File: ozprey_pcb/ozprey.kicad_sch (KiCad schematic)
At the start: 3 parts, among them J1 Conn_01x02, SW43 SW_DPDT_x2, U1 nice_nano

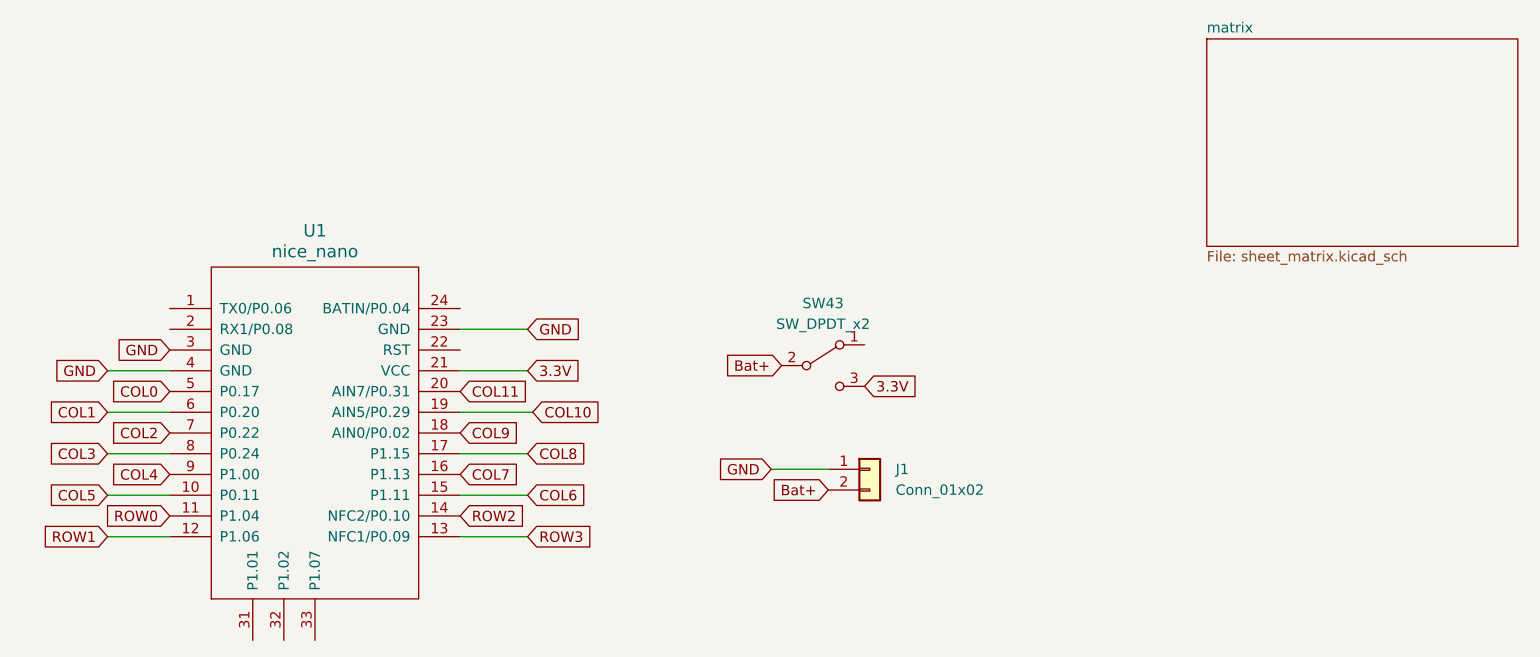
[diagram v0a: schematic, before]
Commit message: rework pcb, remove enclosure & plate folders
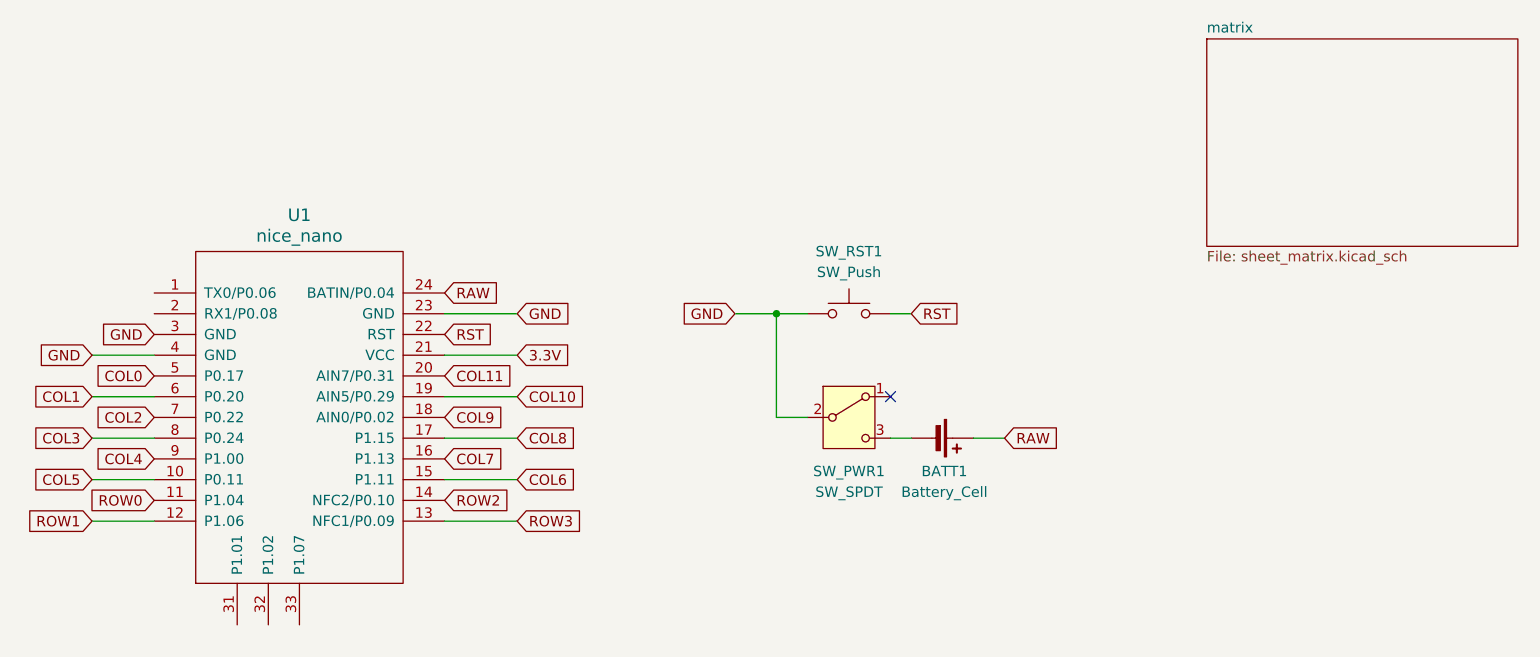
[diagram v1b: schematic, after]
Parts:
- removed J1: Conn_01x02, Connector_JST:JST_ACH_BM02B-ACHSS-GAN-ETF_1x02-1MP_P1.20mm_Vertical, symbol Connector_Generic:Conn_01x02
- removed SW43: SW_DPDT_x2, kapee-keeb-parts:MSK12C02, symbol Switch:SW_SPDT
- added BATT1: Battery_Cell, Keyboard:Battery_pads, symbol Device:Battery_Cell
- added SW_PWR1: SW_SPDT, Button_Switch_SMD:SW_SPDT_PCM12, symbol Switch:SW_SPDT
- added SW_RST1: SW_Push, Button_Switch_SMD:SW_SPST_TL3342, symbol Switch:SW_Push
- U1: footprint kapee-keeb-parts:NiceNano -> ProMicro:nice_nano
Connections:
- net GND: now also SW_PWR1.2 (B), SW_RST1.1
- net RST: now reaches U1.22 (RST)
- net RST: now also SW_RST1.2
- net RAW: now reaches U1.24 (BATIN/P0.04)
- net RAW: now also BATT1.1 (+)
- new net: BATT1.2 (-), SW_PWR1.3 (C)
- no-connect marks 0 -> 1
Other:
- company: (none) -> itsdmd
- title: (none) -> Ozprey
- moved on the sheet: U1

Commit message: update doc
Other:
- sheet matrix renamed Matrix
- added sheet MountingHoles (untitled.kicad_sch)
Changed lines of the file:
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@@
 			(color 0 0 0 0.0000)
 		)
-		(property "Sheetname" "matrix"
-			(at 187.325 24.1295 0)
+		(property "Sheetname" "Matrix"
+			(at 187.325 24.0534 0)
 			(effects
 				(font
@@
 		)
 		(property "Sheetfile" "sheet_matrix.kicad_sch"
-			(at 187.325 50.6735 0)
+			(at 187.325 50.7496 0)
 			(effects
 				(font
+					(size 1.27 1.27)
+				)
+				(justify left top)
+			)
+		)
+		(instances
+			(project "ozprey"
+				(path "/86a516b3-939b-48ee-9a25-d0111c577d06"
+					(page "2")
+				)
+			)
+		)
+	)
+	(sheet
+		(at 187.96 59.69)
+		(size 38.1 24.13)
+		(fields_autoplaced yes)
+		(stroke
+			(width 0.1524)
+			(type solid)
+		)
+		(fill
+			(color 0 0 0 0.0000)
+		)
+		(property "Sheetname" "MountingHoles"
+			(at 187.96 58.9784 0)
+			(effects
+				(font
+					(size 1.27 1.27)
+				)
+				(justify left bottom)
+			)
+		)
+		(property "Sheetfile" "untitled.kicad_sch"
+			(at 187.96 84.4046 0)
+			(effects
+				(font

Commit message: replace power & reset switches
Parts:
- removed SW_PWR1: SW_SPDT, Button_Switch_SMD:SW_SPDT_PCM12, symbol Switch:SW_SPDT
- added SW43: SK12D07VG4, Switch:SK12D07VG4, symbol SK12D07VG4:SK12D07VG4
- SW_RST1: footprint Button_Switch_SMD:SW_SPST_TL3342 -> Switch:KG1
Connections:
- net GND: now also SW_RST1.2, SW43.COM; no longer SW_RST1.1
- net RST: now also SW_RST1.1; no longer SW_RST1.2
- net at BATT1.2 (-): now also SW43.2
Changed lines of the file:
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@@
+		(color 0 0 0 0)
+	)
+	(junction
+		(at 135.89 71.12)
+		(diameter 0)
 		(color 0 0 0 0)
 	)
@@
 	(wire
 		(pts
+			(xy 135.89 71.12) (xy 138.43 71.12)
+		)
+		(stroke
+			(width 0)
+			(type default)
+		)
+	)
+	(wire
+		(pts
 			(xy 93.98 68.58) (xy 102.87 68.58)
 		)
@@
 	(wire
 		(pts
+			(xy 134.62 71.12) (xy 135.89 71.12)
+		)
+		(stroke
+			(width 0)
+			(type default)
+		)
+	)
+	(wire
+		(pts
 			(xy 93.98 78.74) (xy 102.87 78.74)
 		)
@@
 		(pts
 			(xy 50.8 73.66) (xy 58.42 73.66)
-		)
-		(stroke
-			(width 0)
-			(type default)
-		)
-	)
-	(wire
-		(pts
-			(xy 134.62 71.12) (xy 138.43 71.12)
 		)
 		(stroke
@@
 	)
 	(symbol
-		(lib_name "SW_SPDT_1")
-		(lib_id "Switch:SW_SPDT")
-		(at 143.51 71.12 0)
-		(unit 1)
-		(exclude_from_sim no)
-		(in_bom yes)
-		(on_board yes)
-		(dnp no)
-		(property "Reference" "SW_PWR1"
-			(at 143.51 77.724 0)
-			(effects
-				(font
-					(size 1.27 1.27)
-				)
-			)
-		)
-		(property "Value" "SW_SPDT"
-			(at 143.51 80.264 0)
-			(effects
-				(font
-					(size 1.27 1.27)
-				)
-			)
-		)
-		(property "Footprint" "Button_Switch_SMD:SW_SPDT_PCM12"
-			(at 143.51 71.12 0)
-			(effects
-				(font
-					(size 1.27 1.27)
-				)
-				(hide yes)
-			)
-		)
-		(property "Datasheet" "~"
-			(at 143.51 78.74 0)
-			(effects
-				(font
-					(size 1.27 1.27)
-				)
-				(hide yes)
-			)
-		)
-		(property "Description" "Switch, single pole double throw"
-			(at 143.51 71.12 0)
-			(effects
-				(font
-					(size 1.27 1.27)
-				)
-				(hide yes)
-			)
-		)
-		(pin "2"
-		)
-		(pin "1"
-		)
-		(pin "3"
-		)
-		(instances
-			(project ""
-				(path "/86a516b3-939b-48ee-9a25-d0111c577d06"
-					(reference "SW_PWR1")
-					(unit 1)
-				)
-			)
-		)
-	)
-	(symbol
 		(lib_id "nice_nano:nice_nano")
 		(at 76.2 69.85 0)
@@
 		(lib_id "Switch:SW_Push")
 		(at 143.51 58.42 0)
+		(mirror y)
 		(unit 1)
 		(exclude_from_sim no)
@@
 			)
 		)
-		(property "Footprint" "Button_Switch_SMD:SW_SPST_TL3342"
+		(property "Footprint" "Switch:KG1"
 			(at 143.51 53.34 0)
 			(effects
@@
 					(unit 1)
 				)
+			)
+		)
+	)
+	(symbol
+		(lib_id "SK12D07VG4:SK12D07VG4")
+		(at 142.24 72.39 0)
+		(unit 1)
+		(exclude_from_sim no)
+		(in_bom yes)
+		(on_board yes)
+		(dnp no)
+		(property "Reference" "SW43"
+			(at 142.24 77.724 0)
+			(effects
+				(font
+					(size 1.27 1.27)
+				)
+			)
+		)
+		(property "Value" "SK12D07VG4"
+			(at 142.24 80.264 0)
+			(effects
+				(font
+					(size 1.27 1.27)
+				)
+			)
+		)
+		(property "Footprint" "Switch:SK12D07VG4"
+			(at 142.24 80.772 0)
+			(effects
+				(font
+					(size 1.27 1.27)
+				)
+				(justify bottom)
+				(hide yes)
+			)
+		)
+		(property "Datasheet" ""
+			(at 142.24 72.39 0)
+			(effects
+				(font
+					(size 1.27 1.27)
+				)
+				(hide yes)
+			)
+		)
+		(property "Description" ""
+			(at 142.24 72.39 0)
+			(effects
+				(font
+					(size 1.27 1.27)
+				)
+				(hide yes)
+			)
+		)
+		(property "MF" "C&K"
+			(at 142.24 72.39 0)
+			(effects
+				(font
+					(size 1.27 1.27)
+				)
+				(justify bottom)
+				(hide yes)
+			)
+		)
+		(property "Description_1" "\nSwitch Slide ON ON SPDT Side Slide 0.3A 30VDC PC Pins Bracket Mount/Through Hole Bulk\n"
+			(at 142.748 86.614 0)
+			(effects
+				(font
+					(size 1.27 1.27)
+				)
+				(justify bottom)
+				(hide yes)
+			)
+		)
+		(property "Package" "None"
+			(at 142.24 72.39 0)
+			(effects
+				(font
+					(size 1.27 1.27)
+				)
+				(justify bottom)
+				(hide yes)
+			)
+		)
+		(property "Price" "None"
+			(at 142.24 72.39 0)
+			(effects
+				(font
+					(size 1.27 1.27)
+				)
+				(justify bottom)
+				(hide yes)
+			)
+		)
+		(property "SnapEDA_Link" "https://www.snapeda.com/parts/SK12D07VG4/C%2526K/view-part/?ref=snap"
+			(at 142.494 84.836 0)
+			(effects
+				(font
+					(size 1.27 1.27)
+				)
+				(justify bottom)
+				(hide yes)
+			)
+		)
+		(property "MP" "SK12D07VG4"
+			(at 141.986 78.486 0)
+			(effects
+				(font
+					(size 1.27 1.27)
+				)
+				(justify bottom)
+				(hide yes)
+			)
+		)
+		(property "Availability" "Not in stock"
+			(at 142.24 72.39 0)
+			(effects
+				(font
+					(size 1.27 1.27)
+				)
+				(justify bottom)
+				(hide yes)
+			)
+		)
+		(property "Check_prices" "https://www.snapeda.com/parts/SK12D07VG4/C%2526K/view-part/?ref=eda"
+			(at 141.986 82.804 0)
+			(effects
+				(font
+					(size 1.27 1.27)
+				)
+				(justify bottom)
+				(hide yes)
+			)
+		)
+		(pin "COM"
+		)
+		(pin "1"
+		)
+		(pin "2"
+		)
+		(instances
+			(project ""
+				(path "/86a516b3-939b-48ee-9a25-d0111c577d06"
+					(reference "SW43")
+					(unit 1)
+				)

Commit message: major changes, add plate
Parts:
- added SW_RST2: SW_Push, itsdmd:SW-T_SPST_TL3342, symbol Switch:SW_Push
- BATT1: footprint Keyboard:Battery_pads -> itsdmd:Battery_Pads-dual-side
- SW43: footprint Switch:SK12D07VG4 -> itsdmd:SW-S_SK12D07VG4; symbol SK12D07VG4:SK12D07VG4 -> itsdmd:SK12D07VG4
- SW_RST1: footprint Switch:KG1 -> itsdmd:SW-S_7.4x2.6-4pad-smd
- U1: footprint ProMicro:nice_nano -> itsdmd:MCB_nice-nano_flip; symbol nice_nano:nice_nano -> itsdmd:nice_nano; now left out of the parts list
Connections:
- net COL0: now also U1.20 (P0.31-LF); no longer U1.5 (P0.17)
- net COL1: now also U1.19 (P0.29-LF); no longer U1.6 (P0.20)
- net COL10: now also U1.6 (P0.20); no longer U1.19 (AIN5/P0.29)
- net COL11: now also U1.5 (P0.17); no longer U1.20 (AIN7/P0.31)
- net COL2: now also U1.18 (P0.02-LF); no longer U1.7 (P0.22)
- net COL3: now also U1.17 (P1.15-LF); no longer U1.8 (P0.24)
- net COL4: now also U1.16 (P1.13-LF); no longer U1.9 (P1.00)
- net COL5: now also U1.15 (P1.11-LF); no longer U1.10 (P0.11)
- net COL6: now also U1.10 (P0.11); no longer U1.15 (P1.11)
- net COL7: now also U1.9 (P1.00); no longer U1.16 (P1.13)
- net COL8: now also U1.8 (P0.24); no longer U1.17 (P1.15)
- net COL9: now also U1.7 (P0.22); no longer U1.18 (AIN0/P0.02)
- net GND: now also BATT1.2 (-), SW_RST1.1, SW_RST2.1; no longer SW43.COM, SW_RST1.2
- net RAW: now also SW43.COM; no longer BATT1.1 (+)
- net ROW0: now also U1.14 (P0.10-LF); no longer U1.11 (P1.04)
- net ROW1: now also U1.13 (P0.09-LF); no longer U1.12 (P1.06)
- net ROW2: now also U1.11 (P1.04-LF); no longer U1.14 (NFC2/P0.10)
- net ROW3: now also U1.12 (P1.06-LF); no longer U1.13 (NFC1/P0.09)
- net RST: now also SW_RST1.2, SW_RST2.2; no longer SW_RST1.1
- net at SW43.2: now also BATT1.1 (+); no longer BATT1.2 (-)
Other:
- moved on the sheet: BATT1, SW_RST1
